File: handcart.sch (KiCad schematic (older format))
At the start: 50 parts, among them J1 PANEL, J10 FANS, J2 BMS, J3 Raspberry_Pi_2_3, J4 DB9_Female_DCE, J5 CHARGER, J8 POWER, K1 OJE-SH-112DM, Q1 2N7002NXAKR, Q2 NTR5105PT1G, Q3 NTR5105PT1G, Q4 2N7002NXAKR, Q5 NTR5105PT1G, Q6 2N7002NXAKR, Q7 2N7002NXAKR, SW1 SW_SPDT, U1 MCP2515-xSO, U2 MCP2562-E-SN, U3 MAX3232CDR, U4 Tex_DCDC, U5 L7805, Y1 16MHz

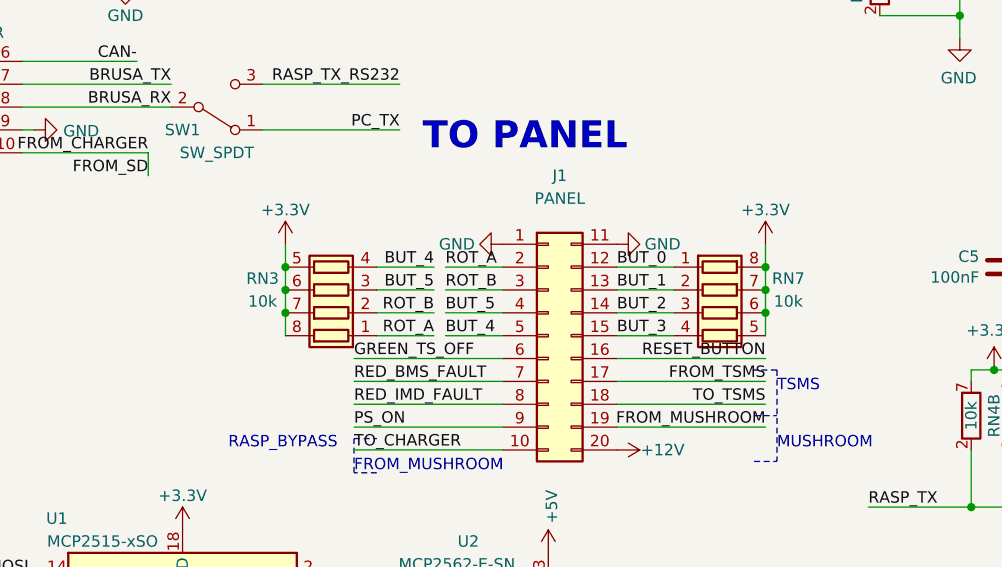
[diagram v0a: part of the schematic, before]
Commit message: added button labels on schematic
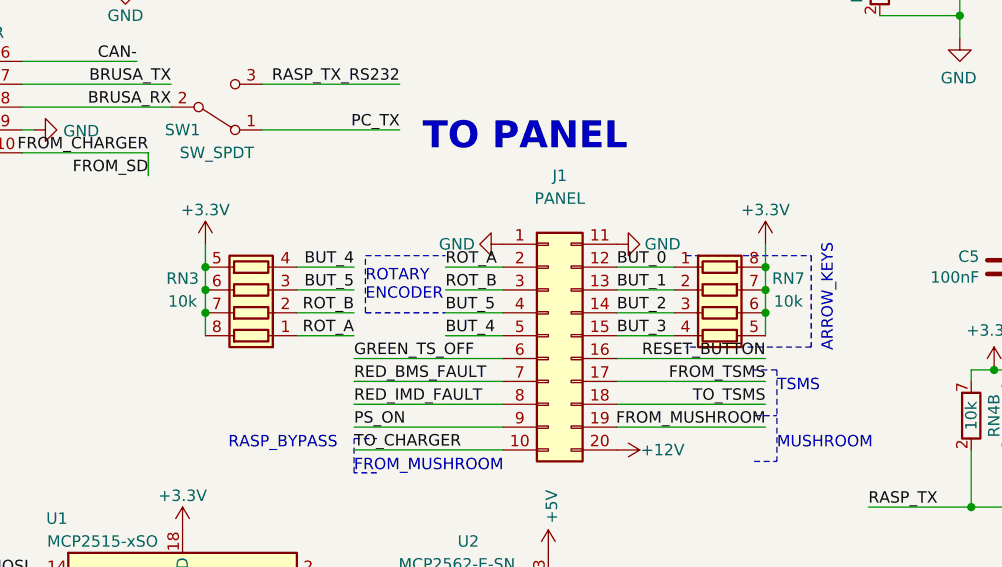
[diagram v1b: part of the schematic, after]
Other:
- note added: "ARROW_KEYS"
- note added: "ROTARY\nENCODER"
- moved on the sheet: RN3
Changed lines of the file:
@@
 L Device:R_Pack04 RN3
 U 1 1 6122C9F1
-P 5000 3100
-F 0 "RN3" V 5050 3400 50  0000 C CNN
-F 1 "10k" V 4950 3400 50  0000 C CNN
-F 2 "Resistor_SMD:R_Array_Convex_4x0612" V 4920 3100 50  0001 C CNN
-F 3 "~" H 5000 3100 50  0001 C CNN
-	1    5000 3100
+P 4650 3100
+F 0 "RN3" V 4700 3400 50  0000 C CNN
+F 1 "10k" V 4600 3400 50  0000 C CNN
+F 2 "Resistor_SMD:R_Array_Convex_4x0612" V 4570 3100 50  0001 C CNN
+F 3 "~" H 4650 3100 50  0001 C CNN
+	1    4650 3100
 	0    -1   -1   0
 $EndComp
@@
 L power:+3.3V #PWR0116
 U 1 1 612976F7
-P 4800 2900
-F 0 "#PWR0116" H 4800 2750 50  0001 C CNN
-F 1 "+3.3V" H 4800 3050 50  0000 C CNN
-F 2 "" H 4800 2900 50  0001 C CNN
-F 3 "" H 4800 2900 50  0001 C CNN
-	1    4800 2900
-	1    0    0    -1
-$EndComp
-Wire Wire Line
-	4800 2900 4800 3000
-Connection ~ 4800 3000
-Wire Wire Line
-	4800 3000 4800 3100
-Connection ~ 4800 3100
-Wire Wire Line
-	4800 3100 4800 3200
-Connection ~ 4800 3200
-Wire Wire Line
-	4800 3200 4800 3300
+P 4450 2900
+F 0 "#PWR0116" H 4450 2750 50  0001 C CNN
+F 1 "+3.3V" H 4450 3050 50  0000 C CNN
+F 2 "" H 4450 2900 50  0001 C CNN
+F 3 "" H 4450 2900 50  0001 C CNN
+	1    4450 2900
+	1    0    0    -1
+$EndComp
+Wire Wire Line
+	4450 2900 4450 3000
+Connection ~ 4450 3000
+Wire Wire Line
+	4450 3000 4450 3100
+Connection ~ 4450 3100
+Wire Wire Line
+	4450 3100 4450 3200
+Connection ~ 4450 3200
+Wire Wire Line
+	4450 3200 4450 3300
 Text Label 5100 3400 0    50   ~ 0
 GREEN_TS_OFF
@@
 Text Label 3500 4650 0    50   ~ 0
 CLK
-Text Label 5450 3300 2    50   ~ 0
+Text Label 5100 3300 2    50   ~ 0
 ROT_A
-Text Label 5450 3200 2    50   ~ 0
+Text Label 5100 3200 2    50   ~ 0
 ROT_B
-Text Label 5450 3000 2    50   ~ 0
+Text Label 5100 3000 2    50   ~ 0
 BUT_4
-Text Label 5450 3100 2    50   ~ 0
+Text Label 5100 3100 2    50   ~ 0
 BUT_5
 Wire Wire Line
-	5450 3100 5200 3100
-Wire Wire Line
-	5200 3300 5450 3300
-Wire Wire Line
-	5450 3200 5200 3200
-Wire Wire Line
-	5450 3000 5200 3000
+	5100 3100 4850 3100
+Wire Wire Line
+	4850 3300 5100 3300
+Wire Wire Line
+	5100 3200 4850 3200
+Wire Wire Line
+	5100 3000 4850 3000
 Text Label 6900 3400 2    50   ~ 0
 RESET_BUTTON
@@
 Text Notes 5400 2500 0    118  ~ 24
 TO PANEL
+Text Notes 7200 2900 3    50   ~ 0
+ARROW_KEYS
+Wire Notes Line
+	6550 2950 7100 2950
+Wire Notes Line
+	7100 2950 7100 3350
+Wire Notes Line
+	7100 3350 6550 3350
+Text Notes 5150 3150 0    50   ~ 0
+ROTARY\nENCODER
+Wire Notes Line
+	5150 3200 5150 2950
+Wire Notes Line
+	5150 2950 5500 2950
+Wire Notes Line
+	5150 3200 5500 3200
 $EndSCHEMATC

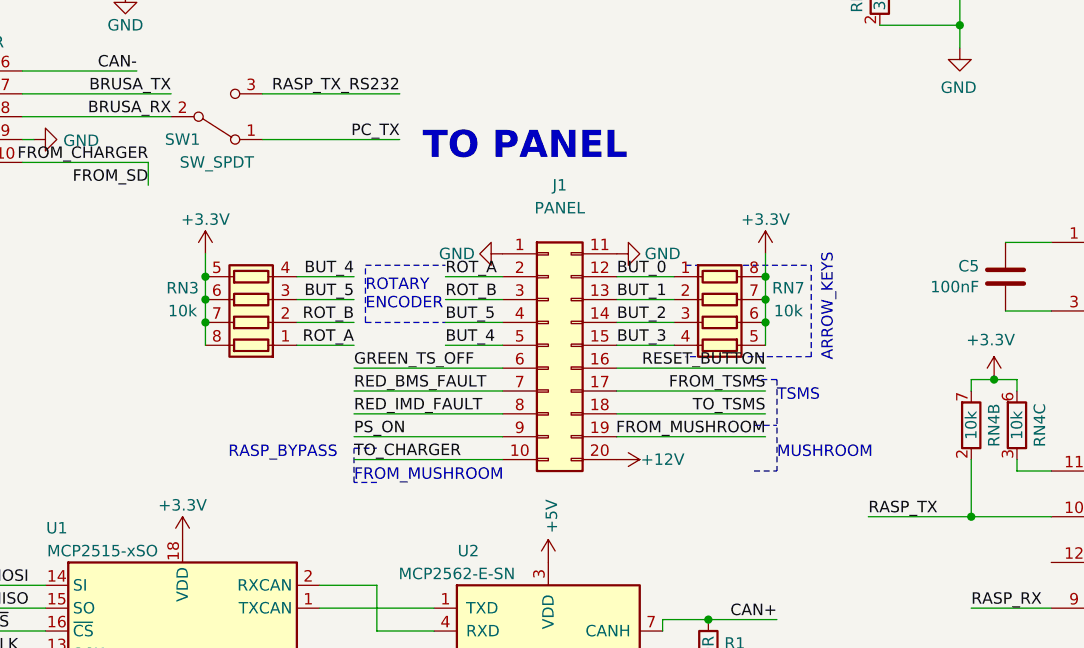
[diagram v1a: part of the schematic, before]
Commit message: added mounting holes
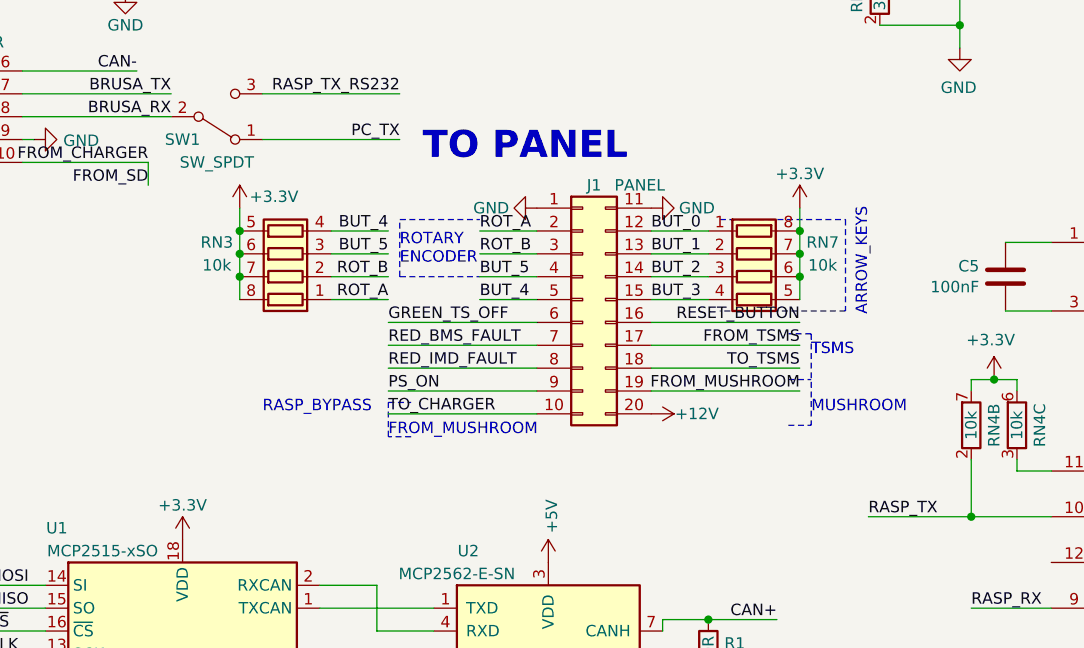
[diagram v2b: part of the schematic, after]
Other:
- moved on the sheet: J1, RN3, RN7

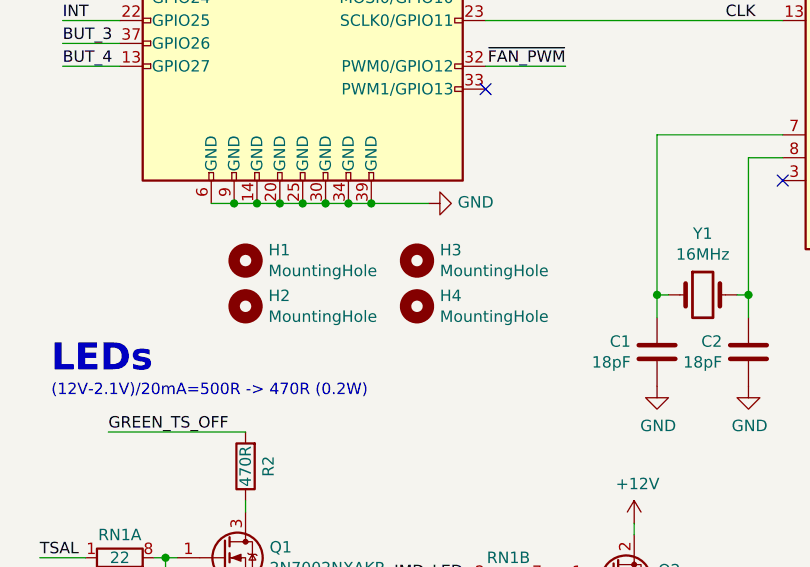
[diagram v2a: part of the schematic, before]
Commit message: added fan hole to pi
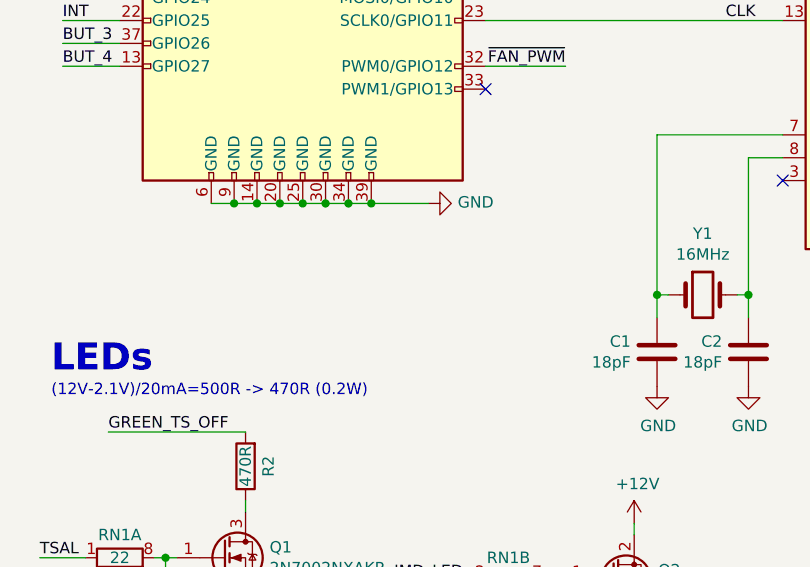
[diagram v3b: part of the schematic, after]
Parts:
- removed H1, H2, H3, H4: MountingHole, handcart:MountingHole_2.75_6.1Free, symbol Mechanical:MountingHole
- J3: footprint Connector_PinHeader_2.54mm:PinHeader_2x20_P2.54mm_Vertical -> handcart:raspberrypi_hat_template
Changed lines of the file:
@@
 F 0 "J3" H 1000 5500 50  0000 C CNN
 F 1 "Raspberry_Pi_2_3" H 1050 5400 50  0000 C CNN
-F 2 "Connector_PinHeader_2.54mm:PinHeader_2x20_P2.54mm_Vertical" H 1650 4150 50  0001 C CNN
+F 2 "handcart:raspberrypi_hat_template" H 1650 4150 50  0001 C CNN
 F 3 "https://www.raspberrypi.org/documentation/hardware/raspberrypi/schematics/rpi_SCH_3bplus_1p0_reduced.pdf" H 1650 4150 50  0001 C CNN
 	1    1650 4150
@@
 Text Notes 5250 6000 0    118  ~ 24
 FANS
-$Comp
-L Mechanical:MountingHole H1
-U 1 1 614D4003
-P 1400 5700
-F 0 "H1" H 1500 5746 50  0000 L CNN
-F 1 "MountingHole" H 1500 5655 50  0000 L CNN
-F 2 "handcart:MountingHole_2.75_6.1Free" H 1400 5700 50  0001 C CNN
-F 3 "~" H 1400 5700 50  0001 C CNN
-	1    1400 5700
-	1    0    0    -1
-$EndComp
-$Comp
-L Mechanical:MountingHole H2
-U 1 1 610579C6
-P 1400 5900
-F 0 "H2" H 1500 5946 50  0000 L CNN
-F 1 "MountingHole" H 1500 5855 50  0000 L CNN
-F 2 "handcart:MountingHole_2.75_6.1Free" H 1400 5900 50  0001 C CNN
-F 3 "~" H 1400 5900 50  0001 C CNN
-	1    1400 5900
-	1    0    0    -1
-$EndComp
-$Comp
-L Mechanical:MountingHole H3
-U 1 1 61057C1F
-P 2150 5700
-F 0 "H3" H 2250 5746 50  0000 L CNN
-F 1 "MountingHole" H 2250 5655 50  0000 L CNN
-F 2 "handcart:MountingHole_2.75_6.1Free" H 2150 5700 50  0001 C CNN
-F 3 "~" H 2150 5700 50  0001 C CNN
-	1    2150 5700
-	1    0    0    -1
-$EndComp
-$Comp
-L Mechanical:MountingHole H4
-U 1 1 61057F0F
-P 2150 5900
-F 0 "H4" H 2250 5946 50  0000 L CNN
-F 1 "MountingHole" H 2250 5855 50  0000 L CNN
-F 2 "handcart:MountingHole_2.75_6.1Free" H 2150 5900 50  0001 C CNN
-F 3 "~" H 2150 5900 50  0001 C CNN
-	1    2150 5900
-	1    0    0    -1
-$EndComp
 Text Label 600  4650 0    50   ~ 0
 INT

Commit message: changed relay, modified gitignore, did the output
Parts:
- removed K1: OJE-SH-112DM, handcart:OJE-SH-112DM, symbol handcart:OJE-SH-112DM
- added K1: EX12U1S, Eagle_Main:EX12U1S, symbol Eagle_Main:EX12U1S
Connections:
- no-connect marks 26 -> 27
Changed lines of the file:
@@
 Sheet 1 1
 Title "Handcart"
-Date "2021-08-08"
+Date "2021-11-11"
 Rev "v2"
 Comp "E-Agle - TRT"
@@
 Text Label 4200 2500 2    50   ~ 0
 FROM_CHARGER
-Wire Wire Line
-	10650 850  10650 800
 $Comp
 L power:GND #PWR037
@@
 Wire Wire Line
 	10550 1600 10550 1450
-Wire Wire Line
-	10650 800  11150 800
 Text Label 550  1100 0    50   ~ 0
 FROM_SD
@@
 	1    1650 1500
 	0    -1   1    0
-$EndComp
-$Comp
-L handcart:OJE-SH-112DM K1
-U 1 1 6113716B
-P 10400 1150
-F 0 "K1" H 10900 1150 50  0000 R CNN
-F 1 "OJE-SH-112DM" H 11400 1250 50  0000 R CNN
-F 2 "handcart:OJE-SH-112DM" H 11675 1200 50  0001 C CNN
-F 3 "https://www.panasonic-electric-works.com/pew/es/downloads/ds_dw_hl_en.pdf" H 10350 1150 50  0001 C CNN
-	1    10400 1150
-	1    0    0    1
 $EndComp
 $Comp
@@
 Wire Wire Line
 	7050 3200 6400 3200
-Wire Wire Line
-	10650 800  10150 800
-Connection ~ 10650 800
 Connection ~ 10150 800
 Text Label 5250 3600 0    50   ~ 0
@@
 Wire Notes Line
 	5300 3000 5650 3000
+$Comp
+L Eagle_Main:EX12U1S K1
+U 1 1 618FFE24
+P 10350 1150
+F 0 "K1" H 10780 1196 50  0000 L CNN
+F 1 "EX12U1S" H 10780 1105 50  0000 L CNN
+F 2 "Eagle_Main:EX12U1S" H 11900 1100 50  0001 C CNN
+F 3 "https://www.mouser.it/datasheet/2/212/1/relay_ex1_ex2_e-844962.pdf" H 10350 1150 50  0001 C CNN
+	1    10350 1150
+	1    0    0    -1
+$EndComp
+Wire Wire Line
+	10150 800  10650 800
+Wire Wire Line
+	10650 850  10650 800
+Connection ~ 10650 800
+Wire Wire Line
+	10650 800  11150 800
+NoConn ~ 10450 850
 $EndSCHEMATC

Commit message: missing holes added
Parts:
- added H1, H2, H3, H4, H5, H6, H7, H8: MountingHole, Eagle_Main:MountingHole_3.2_6.1Free, symbol Mechanical:MountingHole
- J3: footprint handcart:raspberrypi_hat_template -> Eagle_Main:raspberrypi_hat_template
- U4: footprint handcart:Tex_DCDC -> Eagle_Main:Tex_DCDC_horizontal; symbol handcart:Tex_DCDC -> Eagle_Main:Tex_DCDC
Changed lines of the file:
@@
 F 0 "J3" H 1000 5500 50  0000 C CNN
 F 1 "Raspberry_Pi_2_3" H 1050 5400 50  0000 C CNN
-F 2 "handcart:raspberrypi_hat_template" H 1650 4150 50  0001 C CNN
+F 2 "Eagle_Main:raspberrypi_hat_template" H 1650 4150 50  0001 C CNN
 F 3 "https://www.raspberrypi.org/documentation/hardware/raspberrypi/schematics/rpi_SCH_3bplus_1p0_reduced.pdf" H 1650 4150 50  0001 C CNN
 	1    1650 4150
@@
 	4450 7550 4450 7500
 $Comp
-L handcart:Tex_DCDC U4
+L Eagle_Main:Tex_DCDC U4
 U 1 1 611A7401
 P 4100 850
 F 0 "U4" V 4238 72  50  0000 R CNN
 F 1 "Tex_DCDC" V 4147 72  50  0000 R CNN
-F 2 "handcart:Tex_DCDC" H 4000 850 50  0001 C CNN
+F 2 "Eagle_Main:Tex_DCDC_horizontal" H 4000 850 50  0001 C CNN
 F 3 "" H 4000 850 50  0001 C CNN
 	1    4100 850
@@
 	10650 800  11150 800
 NoConn ~ 10450 850
+$Comp
+L Mechanical:MountingHole H6
+U 1 1 619A6886
+P 10450 6100
+F 0 "H6" H 10550 6146 50  0000 L CNN
+F 1 "MountingHole" H 10550 6055 50  0000 L CNN
+F 2 "Eagle_Main:MountingHole_3.2_6.1Free" H 10450 6100 50  0001 C CNN
+F 3 "~" H 10450 6100 50  0001 C CNN
+	1    10450 6100
+	1    0    0    -1
+$EndComp
+$Comp
+L Mechanical:MountingHole H7
+U 1 1 619A6D58
+P 10450 6250
+F 0 "H7" H 10550 6296 50  0000 L CNN
+F 1 "MountingHole" H 10550 6205 50  0000 L CNN
+F 2 "Eagle_Main:MountingHole_3.2_6.1Free" H 10450 6250 50  0001 C CNN
+F 3 "~" H 10450 6250 50  0001 C CNN
+	1    10450 6250
+	1    0    0    -1
+$EndComp
+$Comp
+L Mechanical:MountingHole H8
+U 1 1 619A6FE9
+P 10450 6400
+F 0 "H8" H 10550 6446 50  0000 L CNN
+F 1 "MountingHole" H 10550 6355 50  0000 L CNN
+F 2 "Eagle_Main:MountingHole_3.2_6.1Free" H 10450 6400 50  0001 C CNN
+F 3 "~" H 10450 6400 50  0001 C CNN
+	1    10450 6400
+	1    0    0    -1
+$EndComp
+$Comp
+L Mechanical:MountingHole H5
+U 1 1 619A7249
+P 10450 5950
+F 0 "H5" H 10550 5996 50  0000 L CNN
+F 1 "MountingHole" H 10550 5905 50  0000 L CNN
+F 2 "Eagle_Main:MountingHole_3.2_6.1Free" H 10450 5950 50  0001 C CNN
+F 3 "~" H 10450 5950 50  0001 C CNN
+	1    10450 5950
+	1    0    0    -1
+$EndComp
+$Comp
+L Mechanical:MountingHole H2
+U 1 1 619B72FA
+P 9750 6100
+F 0 "H2" H 9850 6146 50  0000 L CNN
+F 1 "MountingHole" H 9850 6055 50  0000 L CNN
+F 2 "Eagle_Main:MountingHole_3.2_6.1Free" H 9750 6100 50  0001 C CNN
+F 3 "~" H 9750 6100 50  0001 C CNN
+	1    9750 6100
+	1    0    0    -1
+$EndComp
+$Comp
+L Mechanical:MountingHole H3
+U 1 1 619B7300
+P 9750 6250
+F 0 "H3" H 9850 6296 50  0000 L CNN
+F 1 "MountingHole" H 9850 6205 50  0000 L CNN
+F 2 "Eagle_Main:MountingHole_3.2_6.1Free" H 9750 6250 50  0001 C CNN
+F 3 "~" H 9750 6250 50  0001 C CNN
+	1    9750 6250
+	1    0    0    -1
+$EndComp
+$Comp
+L Mechanical:MountingHole H4
+U 1 1 619B7306
+P 9750 6400
+F 0 "H4" H 9850 6446 50  0000 L CNN
+F 1 "MountingHole" H 9850 6355 50  0000 L CNN
+F 2 "Eagle_Main:MountingHole_3.2_6.1Free" H 9750 6400 50  0001 C CNN
+F 3 "~" H 9750 6400 50  0001 C CNN
+	1    9750 6400
+	1    0    0    -1
+$EndComp
+$Comp
+L Mechanical:MountingHole H1
+U 1 1 619B730C
+P 9750 5950
+F 0 "H1" H 9850 5996 50  0000 L CNN
+F 1 "MountingHole" H 9850 5905 50  0000 L CNN
+F 2 "Eagle_Main:MountingHole_3.2_6.1Free" H 9750 5950 50  0001 C CNN
+F 3 "~" H 9750 5950 50  0001 C CNN
+	1    9750 5950
+	1    0    0    -1
+$EndComp
 $EndSCHEMATC

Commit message: renamed SD nets
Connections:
- net labels added: SD_BMS_IN, SD_BMS_OUT, SD_END, SD_END_HV, SD_FROM_CHARGER, SD_FROM_MUSHROOM, SD_TO_CHARGER
- net labels removed: FROM_CHARGER, FROM_MUSHROOM, FROM_SD, FROM_TSMS, FROM_TSMS_HV, TO_CHARGER, TO_TSMS
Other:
- note added: "SD_FROM_MUSHROOM"
- note added: "SD_START"
- note removed: "FROM_MUSHROOM"
- moved on the sheet: SW1
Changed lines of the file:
@@
 	1150 800  900  800
 Text Label 550  1200 0    50   ~ 0
-TO_TSMS
+SD_BMS_OUT
 Text Label 550  2000 0    50   ~ 0
-FROM_TSMS
+SD_END
 Wire Wire Line
 	550  1100 1150 1100
@@
 Wire Wire Line
 	3750 7150 4100 7150
-Text Label 2650 2400 0    50   ~ 0
+Text Label 2600 2400 0    50   ~ 0
 PON
-Text Label 2650 2500 0    50   ~ 0
-TO_CHARGER
-Text Label 4200 2500 2    50   ~ 0
-FROM_CHARGER
+Text Label 2600 2500 0    50   ~ 0
+SD_TO_CHARGER
+Text Label 4350 2500 2    50   ~ 0
+SD_FROM_CHARGER
 $Comp
 L power:GND #PWR037
@@
 Connection ~ 10150 2100
 Text Label 11150 800  2    50   ~ 0
-TO_CHARGER
+SD_TO_CHARGER
 Wire Wire Line
 	10550 1600 10550 1450
 Text Label 550  1100 0    50   ~ 0
-FROM_SD
-Text Label 4200 2600 2    50   ~ 0
-FROM_SD
-Text Label 7050 3400 2    50   ~ 0
-TO_TSMS
-Text Label 7050 3300 2    50   ~ 0
-FROM_TSMS
+SD_BMS_IN
+Text Label 4350 2600 2    50   ~ 0
+SD_BMS_IN
+Text Label 7200 3400 2    50   ~ 0
+SD_BMS_OUT
+Text Label 7200 3300 2    50   ~ 0
+SD_END
 Text Notes 8900 700  0    118  ~ 24
 SHUTDOWN
@@
 L power:+12V #PWR011
 U 1 1 61092FF4
-P 2600 2300
-F 0 "#PWR011" H 2600 2150 50  0001 C CNN
-F 1 "+12V" V 2615 2428 50  0000 L CNN
-F 2 "" H 2600 2300 50  0001 C CNN
-F 3 "" H 2600 2300 50  0001 C CNN
-	1    2600 2300
+P 2550 2300
+F 0 "#PWR011" H 2550 2150 50  0001 C CNN
+F 1 "+12V" V 2600 2350 50  0000 L CNN
+F 2 "" H 2550 2300 50  0001 C CNN
+F 3 "" H 2550 2300 50  0001 C CNN
+	1    2550 2300
 	0    -1   -1   0
 $EndComp
@@
 Text Label 4300 2200 2    50   ~ 0
 BRUSA_TX
-Text Label 2650 2300 0    50   ~ 0
+Text Label 2600 2300 0    50   ~ 0
 AUX
 $Comp
@@
 	8450 1500 8450 1400
 Text Label 8050 700  0    50   ~ 0
-FROM_TSMS
+SD_END
 Wire Wire Line
 	8050 700  8450 700
@@
 	3650 2200 4300 2200
 Wire Wire Line
-	4300 2300 3650 2300
+	4350 2300 3650 2300
 Wire Wire Line
 	3700 2400 3650 2400
 Wire Wire Line
-	2600 2300 3150 2300
-Wire Wire Line
-	2650 2400 3150 2400
-Wire Wire Line
-	3150 2100 2650 2100
+	2550 2300 3150 2300
+Wire Wire Line
+	2600 2400 3150 2400
+Wire Wire Line
+	3150 2100 2600 2100
 Wire Wire Line
 	4150 2100 3650 2100
 Wire Wire Line
-	3150 2500 2650 2500
+	3150 2500 2600 2500
 $Comp
 L Interface_CAN_LIN:MCP2562-E-SN U2
@@
 L Switch:SW_SPDT SW1
 U 1 1 6103A16F
-P 4500 2300
-F 0 "SW1" H 4350 2400 50  0000 C CNN
-F 1 "SW_SPDT" H 4500 2500 50  0000 C CNN
-F 2 "Button_Switch_THT:SW_E-Switch_EG1224_SPDT_Angled" H 4500 2300 50  0001 C CNN
-F 3 "~" H 4500 2300 50  0001 C CNN
-	1    4500 2300
+P 4550 2300
+F 0 "SW1" H 4400 2400 50  0000 C CNN
+F 1 "SW_SPDT" H 4550 2500 50  0000 C CNN
+F 2 "Button_Switch_THT:SW_E-Switch_EG1224_SPDT_Angled" H 4550 2300 50  0001 C CNN
+F 3 "~" H 4550 2300 50  0001 C CNN
+	1    4550 2300
 	1    0    0    1
 $EndComp
@@
 PC_TX
 Wire Wire Line
-	5300 2400 4700 2400
+	5300 2400 4750 2400
 Text Label 5900 550  3    50   ~ 0
 PC_TX
@@
 RASP_TX_RS232
 Wire Wire Line
-	4700 2200 5300 2200
+	4750 2200 5300 2200
 $Comp
 L power:GND #PWR014
@@
 NoConn ~ 5500 950
 Wire Wire Line
-	7050 3400 6400 3400
-Wire Wire Line
-	7050 3300 6400 3300
+	7200 3400 6400 3400
+Wire Wire Line
+	7200 3300 6400 3300
 Wire Notes Line
-	7000 3450 7100 3450
+	7150 3450 7250 3450
 Wire Notes Line
-	7100 3250 7000 3250
-Text Notes 7100 3350 0    50   ~ 0
+	7250 3250 7150 3250
+Text Notes 7250 3350 0    50   ~ 0
 TSMS
-Text Label 11250 1600 2    50   ~ 0
-FROM_MUSHROOM
 Wire Wire Line
 	11250 1600 10550 1600
@@
 	0    1    -1   0
 $EndComp
-Text Label 7050 3500 2    50   ~ 0
-FROM_MUSHROOM
-Wire Wire Line
-	7050 3500 6400 3500
+Wire Wire Line
+	7200 3500 6400 3500
 Wire Notes Line
-	7000 3650 7100 3650
-Text Notes 7100 3600 0    50   ~ 0
+	7150 3650 7250 3650
+Text Notes 7250 3600 0    50   ~ 0
 MUSHROOM
 Wire Notes Line
-	7100 3250 7100 3650
+	7250 3250 7250 3650
 Text Label 5250 3500 0    50   ~ 0
 PS_ON
@@
 Text Label 4150 2100 2    50   ~ 0
 CAN-
-Text Label 2650 2100 0    50   ~ 0
+Text Label 2600 2100 0    50   ~ 0
 CAN+
 $Comp
@@
 $EndComp
 Wire Wire Line
-	4200 2500 3650 2500
-Wire Wire Line
-	4200 2600 4200 2500
+	4350 2500 3650 2500
+Wire Wire Line
+	4350 2600 4350 2500
 Text Label 3500 4450 0    50   ~ 0
 MISO
@@
 Wire Wire Line
 	5250 2800 5000 2800
-Text Label 7050 3200 2    50   ~ 0
+Text Label 7200 3200 2    50   ~ 0
 RESET_BUTTON
 Wire Wire Line
-	7050 3200 6400 3200
+	7200 3200 6400 3200
 Connection ~ 10150 800
 Text Label 5250 3600 0    50   ~ 0
-TO_CHARGER
+SD_TO_CHARGER
 Wire Wire Line
 	5250 3600 5900 3600
-Text Notes 5250 3700 0    50   ~ 0
-FROM_MUSHROOM
 Wire Notes Line
 	5350 3700 5250 3700
@@
 	950  2000 1000 2000
 Text Label 1950 2000 2    50   ~ 0
-FROM_TSMS_HV
+SD_END_HV
 Wire Wire Line
 	1950 2000 1350 2000
 Text Label 550  1300 0    50   ~ 0
-FROM_TSMS_HV
+SD_END_HV
 Wire Wire Line
 	550  1300 1150 1300
@@
 	1    0    0    -1
 $EndComp
+Text Notes 7200 3650 2    50   ~ 0
+SD_START
+Text Label 7200 3500 2    50   ~ 0
+SD_FROM_MUSHROOM
+Text Label 11250 1600 2    50   ~ 0
+SD_FROM_MUSHROOM
+Text Notes 5250 3700 0    50   ~ 0
+SD_FROM_MUSHROOM
 $EndSCHEMATC
